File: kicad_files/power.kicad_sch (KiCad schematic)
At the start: 23 parts, among them J8 Conn_01x02_Socket, Q1 Q_PMOS_GSD, Q2 Q_PMOS_GSD, U11 LT1963AxST-3.3, U12 AP63205WU

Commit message: reset symbol annotations
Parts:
- renumbered C61 to C53, C62 to C54, C63 to C55, C64 to C56, C65 to C57, C66 to C58, C67 to C59, C68 to C60, C69 to C61, C70 to C62, C71 to C63, R25 to R22, R26 to R23, R27 to R24, R28 to R25
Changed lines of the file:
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@@
 		(dnp no)
 		(fields_autoplaced yes)
-		(property "Reference" "C70"
+		(property "Reference" "C62"
 			(at 161.29 127.0062 0)
 			(show_name no)
@@
 			(project "versorlite"
 				(path "/1a230af0-0a74-48f7-8607-b087121dda49/31c1824a-552d-4de4-ae9b-4526af07be04"
-					(reference "C70")
+					(reference "C62")
 					(unit 1)
 				)
@@
 		(dnp no)
 		(fields_autoplaced yes)
-		(property "Reference" "C62"
+		(property "Reference" "C54"
 			(at 46.9965 59.69 0)
 			(show_name no)
@@
 			(project "versorlite"
 				(path "/1a230af0-0a74-48f7-8607-b087121dda49/31c1824a-552d-4de4-ae9b-4526af07be04"
-					(reference "C62")
+					(reference "C54")
 					(unit 1)
 				)
@@
 		(dnp no)
 		(fields_autoplaced yes)
-		(property "Reference" "C68"
+		(property "Reference" "C60"
 			(at 107.95 134.6135 0)
 			(show_name no)
@@
 			(project "versorlite"
 				(path "/1a230af0-0a74-48f7-8607-b087121dda49/31c1824a-552d-4de4-ae9b-4526af07be04"
-					(reference "C68")
+					(reference "C60")
 					(unit 1)
 				)
@@
 		(dnp no)
 		(fields_autoplaced yes)
-		(property "Reference" "C67"
+		(property "Reference" "C59"
 			(at 107.95 124.4535 0)
 			(show_name no)
@@
 			(project "versorlite"
 				(path "/1a230af0-0a74-48f7-8607-b087121dda49/31c1824a-552d-4de4-ae9b-4526af07be04"
-					(reference "C67")
+					(reference "C59")
 					(unit 1)
 				)
@@
 		(dnp no)
 		(fields_autoplaced yes)
-		(property "Reference" "R25"
+		(property "Reference" "R22"
 			(at 54.61 154.9399 0)
 			(show_name no)
@@
 			(project "versorlite"
 				(path "/1a230af0-0a74-48f7-8607-b087121dda49/31c1824a-552d-4de4-ae9b-4526af07be04"
-					(reference "R25")
+					(reference "R22")
 					(unit 1)
 				)
@@
 		(dnp no)
 		(fields_autoplaced yes)
-		(property "Reference" "R28"
+		(property "Reference" "R25"
 			(at 180.34 143.5099 0)
 			(show_name no)
@@
 			(project "versorlite"
 				(path "/1a230af0-0a74-48f7-8607-b087121dda49/31c1824a-552d-4de4-ae9b-4526af07be04"
-					(reference "R28")
+					(reference "R25")
 					(unit 1)
 				)
@@
 		(dnp no)
 		(fields_autoplaced yes)
-		(property "Reference" "C61"
+		(property "Reference" "C53"
 			(at 46.9838 49.53 0)
 			(show_name no)
@@
 			(project "versorlite"
 				(path "/1a230af0-0a74-48f7-8607-b087121dda49/31c1824a-552d-4de4-ae9b-4526af07be04"
-					(reference "C61")
+					(reference "C53")
 					(unit 1)
 				)
@@
 		(dnp no)
 		(fields_autoplaced yes)
-		(property "Reference" "C69"
+		(property "Reference" "C61"
 			(at 151.13 126.9935 0)
 			(show_name no)
@@
 			(project "versorlite"
 				(path "/1a230af0-0a74-48f7-8607-b087121dda49/31c1824a-552d-4de4-ae9b-4526af07be04"
-					(reference "C69")
+					(reference "C61")
 					(unit 1)
 				)
@@
 		(dnp no)
 		(fields_autoplaced yes)
-		(property "Reference" "C66"
+		(property "Reference" "C58"
 			(at 97.79 124.4662 0)
 			(show_name no)
@@
 			(project "versorlite"
 				(path "/1a230af0-0a74-48f7-8607-b087121dda49/31c1824a-552d-4de4-ae9b-4526af07be04"
-					(reference "C66")
+					(reference "C58")
 					(unit 1)
 				)
@@
 		(dnp no)
 		(fields_autoplaced yes)
-		(property "Reference" "C63"
+		(property "Reference" "C55"
 			(at 45.7136 83.82 90)
 			(show_name no)
@@
 			(project "versorlite"
 				(path "/1a230af0-0a74-48f7-8607-b087121dda49/31c1824a-552d-4de4-ae9b-4526af07be04"
-					(reference "C63")
+					(reference "C55")
 					(unit 1)
 				)
@@
 		(in_pos_files yes)
 		(dnp no)
-		(property "Reference" "C71"
+		(property "Reference" "C63"
 			(at 163.83 138.938 0)
 			(show_name no)
@@
 			(project "versorlite"
 				(path "/1a230af0-0a74-48f7-8607-b087121dda49/31c1824a-552d-4de4-ae9b-4526af07be04"
-					(reference "C71")
+					(reference "C63")
 					(unit 1)
 				)
@@
 		(dnp no)
 		(fields_autoplaced yes)
-		(property "Reference" "C64"
+		(property "Reference" "C56"
 			(at 45.7263 93.98 90)
 			(show_name no)
@@
 			(project "versorlite"
 				(path "/1a230af0-0a74-48f7-8607-b087121dda49/31c1824a-552d-4de4-ae9b-4526af07be04"
-					(reference "C64")
+					(reference "C56")
 					(unit 1)
 				)
@@
 		(dnp no)
 		(fields_autoplaced yes)
-		(property "Reference" "R27"
+		(property "Reference" "R24"
 			(at 180.34 135.8899 0)
 			(show_name no)
@@
 			(project "versorlite"
 				(path "/1a230af0-0a74-48f7-8607-b087121dda49/31c1824a-552d-4de4-ae9b-4526af07be04"
-					(reference "R27")
+					(reference "R24")
 					(unit 1)
 				)
@@
 		(in_pos_files yes)
 		(dnp no)
-		(property "Reference" "R26"
+		(property "Reference" "R23"
 			(at 68.58 151.13 0)
 			(show_name no)
@@
 			(project "versorlite"
 				(path "/1a230af0-0a74-48f7-8607-b087121dda49/31c1824a-552d-4de4-ae9b-4526af07be04"
-					(reference "R26")
+					(reference "R23")
 					(unit 1)
 				)
@@
 		(dnp no)
 		(fields_autoplaced yes)
-		(property "Reference" "C65"
+		(property "Reference" "C57"
 			(at 80.01 124.4662 0)
 			(show_name no)
@@
 			(project "versorlite"
 				(path "/1a230af0-0a74-48f7-8607-b087121dda49/31c1824a-552d-4de4-ae9b-4526af07be04"
-					(reference "C65")
-					(unit 1)
-				)
+					(reference "C57")
+					(unit 1)
+				)

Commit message: make schematic changes
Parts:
- removed Q2: Q_PMOS_GSD, symbol Transistor_FET:Q_PMOS_GSD
- removed R23: 100Ω, symbol Device:R_Small_US
- added D8: D_Schottky_Small, symbol Device:D_Schottky_Small
- added SW3: SW_SPST, symbol Switch:SW_SPST
- Q1: value Q_PMOS_GSD -> JMTQ55P02A; footprint (none) -> Package_DFN_QFN:DFN-8-1EP_3x3mm_P0.65mm_EP1.6x2.56mm_ThermalVias
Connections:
- net +9V: now also SW3.2 (B); no longer F1.1
- net +VBUS: now also Q1.1 (G)
- net at C61.1, C62.2, C63.1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: now also D8.1 (K)
- net at F1.2: now also D8.2 (A)
- new net: F1.1, SW3.1 (A)
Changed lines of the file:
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@@
 	)
 	(junction
-		(at 193.04 142.24)
-		(diameter 0)
-		(color 0 0 0 0)
-	)
-	(junction
 		(at 182.88 134.62)
 		(diameter 0)
@@
 	(wire
 		(pts
+			(xy 63.5 147.32) (xy 63.5 152.4)
+		)
+		(stroke
+			(width 0)
+			(type default)
+		)
+	)
+	(wire
+		(pts
 			(xy 48.26 57.15) (xy 50.8 57.15)
 		)
@@
 	(wire
 		(pts
-			(xy 182.88 134.62) (xy 187.96 134.62)
+			(xy 182.88 134.62) (xy 190.5 134.62)
+		)
+		(stroke
+			(width 0)
+			(type default)
+		)
+	)
+	(wire
+		(pts
+			(xy 195.58 134.62) (xy 199.39 134.62)
 		)
 		(stroke
@@
 	(wire
 		(pts
-			(xy 198.12 134.62) (xy 199.39 134.62)
-		)
-		(stroke
-			(width 0)
-			(type default)
-		)
-	)
-	(wire
-		(pts
 			(xy 105.41 139.7) (xy 116.84 139.7)
 		)
@@
 	(symbol
 		(lib_id "power:+9V")
-		(at 210.82 134.62 270)
+		(at 220.98 134.62 270)
 		(unit 1)
 		(body_style 1)
@@
 		(fields_autoplaced yes)
 		(property "Reference" "#PWR091"
-			(at 207.01 134.62 0)
+			(at 217.17 134.62 0)
 			(hide yes)
 			(show_name no)
@@
 		)
 		(property "Value" "+9V"
-			(at 214.63 134.6199 90)
+			(at 224.79 134.6199 90)
 			(show_name no)
 			(do_not_autoplace no)
@@
 		)
 		(property "Footprint" ""
-			(at 210.82 134.62 0)
+			(at 220.98 134.62 0)
 			(hide yes)
 			(show_name no)
@@
 		)
 		(property "Datasheet" ""
-			(at 210.82 134.62 0)
+			(at 220.98 134.62 0)
 			(hide yes)
 			(show_name no)
@@
 		)
 		(property "Description" "Power symbol creates a global label with name \"+9V\""
-			(at 210.82 134.62 0)
+			(at 220.98 134.62 0)
 			(hide yes)
 			(show_name no)
@@
 	)
 	(symbol
+		(lib_id "Device:D_Schottky_Small")
+		(at 193.04 134.62 0)
+		(unit 1)
+		(body_style 1)
+		(exclude_from_sim no)
+		(in_bom yes)
+		(on_board yes)
+		(in_pos_files yes)
+		(dnp no)
+		(property "Reference" "D8"
+			(at 191.008 131.826 90)
+			(show_name no)
+			(do_not_autoplace no)
+			(effects
+				(font
+					(size 1.27 1.27)
+				)
+				(justify left)
+			)
+		)
+		(property "Value" "D_Schottky_Small"
+			(at 192.786 131.826 90)
+			(show_name no)
+			(do_not_autoplace no)
+			(effects
+				(font
+					(size 1.27 1.27)
+				)
+				(justify left)
+			)
+		)
+		(property "Footprint" ""
+			(at 193.04 134.62 90)
+			(hide yes)
+			(show_name no)
+			(do_not_autoplace no)
+			(effects
+				(font
+					(size 1.27 1.27)
+				)
+			)
+		)
+		(property "Datasheet" ""
+			(at 193.04 134.62 90)
+			(hide yes)
+			(show_name no)
+			(do_not_autoplace no)
+			(effects
+				(font
+					(size 1.27 1.27)
+				)
+			)
+		)
+		(property "Description" "Schottky diode, small symbol"
+			(at 193.04 134.62 0)
+			(hide yes)
+			(show_name no)
+			(do_not_autoplace no)
+			(effects
+				(font
+					(size 1.27 1.27)
+				)
+			)
+		)
+		(pin "1"
+		)
+		(pin "2"
+		)
+		(instances
+			(project "versorlite"
+				(path "/1a230af0-0a74-48f7-8607-b087121dda49/31c1824a-552d-4de4-ae9b-4526af07be04"
+					(reference "D8")
+					(unit 1)
+				)
+			)
+		)
+	)
+	(symbol
 		(lib_id "Device:C_Small")
 		(at 45.72 57.15 90)
@@
 			)
 		)
-		(property "Value" "Q_PMOS_GSD"
+		(property "Value" "JMTQ55P02A"
 			(at 63.5 135.89 90)
 			(show_name no)
@@
 			)
 		)
-		(property "Footprint" ""
+		(property "Footprint" "Package_DFN_QFN:DFN-8-1EP_3x3mm_P0.65mm_EP1.6x2.56mm_ThermalVias"
 			(at 60.96 137.16 0)
 			(hide yes)
@@
 	)
 	(symbol
-		(lib_id "Transistor_FET:Q_PMOS_GSD")
-		(at 193.04 137.16 90)
-		(unit 1)
-		(body_style 1)
-		(exclude_from_sim no)
-		(in_bom yes)
-		(on_board yes)
-		(in_pos_files yes)
-		(dnp no)
-		(fields_autoplaced yes)
-		(property "Reference" "Q2"
-			(at 193.04 128.27 90)
-			(show_name no)
-			(do_not_autoplace no)
-			(effects
-				(font
-					(size 1.27 1.27)
-				)
-			)
-		)
-		(property "Value" "Q_PMOS_GSD"
-			(at 193.04 130.81 90)
-			(show_name no)
-			(do_not_autoplace no)
-			(effects
-				(font
-					(size 1.27 1.27)
-				)
-			)
-		)
-		(property "Footprint" ""
-			(at 190.5 132.08 0)
-			(hide yes)
-			(show_name no)
-			(do_not_autoplace no)
-			(effects
-				(font
-					(size 1.27 1.27)
-				)
-			)
-		)
-		(property "Datasheet" ""
-			(at 193.04 137.16 0)
-			(hide yes)
-			(show_name no)
-			(do_not_autoplace no)
-			(effects
-				(font
-					(size 1.27 1.27)
-				)
-			)
-		)
-		(property "Description" "P-MOSFET transistor, gate/source/drain"
-			(at 193.04 137.16 0)
-			(hide yes)
-			(show_name no)
-			(do_not_autoplace no)
-			(effects
-				(font
-					(size 1.27 1.27)
-				)
-			)
-		)
-		(pin "3"
-		)
-		(pin "1"
-		)
-		(pin "2"
-		)
-		(instances
-			(project "versorlite"
-				(path "/1a230af0-0a74-48f7-8607-b087121dda49/31c1824a-552d-4de4-ae9b-4526af07be04"
-					(reference "Q2")
-					(unit 1)
-				)
-			)
-		)
-	)
-	(symbol
 		(lib_id "power:GND")
 		(at 196.85 142.24 90)
@@
 	)
 	(symbol
-		(lib_id "Device:R_Small_US")
-		(at 63.5 149.86 0)
+		(lib_id "power:+3.3V")
+		(at 40.64 38.1 0)
 		(unit 1)
 		(body_style 1)
@@
 		(in_pos_files yes)
 		(dnp no)
-		(property "Reference" "R23"
-			(at 68.58 151.13 0)
+		(property "Reference" "#PWR085"
+			(at 40.64 41.91 0)
+			(hide yes)
 			(show_name no)
 			(do_not_autoplace no)
@@
 			)
 		)
-		(property "Value" "100Ω"
-			(at 68.58 148.59 0)
+		(property "Value" "+3.3V_MAIN"
+			(at 40.386 33.782 0)
 			(show_name no)
 			(do_not_autoplace no)
@@
 		)
 		(property "Footprint" ""
-			(at 63.5 149.86 0)
+			(at 40.64 38.1 0)
 			(hide yes)
 			(show_name no)
@@
 		)
 		(property "Datasheet" ""
-			(at 63.5 149.86 0)
+			(at 40.64 38.1 0)
 			(hide yes)
 			(show_name no)
@@
 			)
 		)
-		(property "Description" "Resistor, small US symbol"
-			(at 63.5 149.86 0)
+		(property "Description" "Power symbol creates a global label with name \"+3.3V\""
+			(at 40.64 38.1 0)
 			(hide yes)
 			(show_name no)
@@
 			)
 		)
-		(pin "2"
-		)
 		(pin "1"
 		)
@@
 			(project "versorlite"
 				(path "/1a230af0-0a74-48f7-8607-b087121dda49/31c1824a-552d-4de4-ae9b-4526af07be04"
-					(reference "R23")
+					(reference "#PWR085")
 					(unit 1)
 				)
@@
 	)
 	(symbol
-		(lib_id "power:+3.3V")
-		(at 40.64 38.1 0)
+		(lib_id "Device:C_Small")
+		(at 77.47 125.73 0)
 		(unit 1)
 		(body_style 1)
@@
 		(in_pos_files yes)
 		(dnp no)
-		(property "Reference" "#PWR085"
-			(at 40.64 41.91 0)
-			(hide yes)
+		(fields_autoplaced yes)
+		(property "Reference" "C57"
+			(at 80.01 124.4662 0)
 			(show_name no)
 			(do_not_autoplace no)
@@
 					(size 1.27 1.27)
 				)
+				(justify left)
 			)
 		)
-		(property "Value" "+3.3V_MAIN"
-			(at 40.386 33.782 0)
+		(property "Value" "100μf"
+			(at 80.01 127.0062 0)
 			(show_name no)
 			(do_not_autoplace no)
@@
 					(size 1.27 1.27)
 				)
+				(justify left)
 			)
 		)
-		(property "Footprint" ""
-			(at 40.64 38.1 0)
+		(property "Footprint" "Capacitor_Tantalum_SMD:CP_EIA-3528-21_Kemet-B"
+			(at 77.47 125.73 0)
 			(hide yes)
 			(show_name no)
@@
 		)
 		(property "Datasheet" ""
-			(at 40.64 38.1 0)
+			(at 77.47 125.73 0)
 			(hide yes)
 			(show_name no)
@@
 			)
 		)
-		(property "Description" "Power symbol creates a global label with name \"+3.3V\""
-			(at 40.64 38.1 0)
+		(property "Description" "Unpolarized capacitor, small symbol"
+			(at 77.47 125.73 0)
 			(hide yes)
 			(show_name no)
@@
 		(pin "1"
 		)
+		(pin "2"
+		)
 		(instances
 			(project "versorlite"
 				(path "/1a230af0-0a74-48f7-8607-b087121dda49/31c1824a-552d-4de4-ae9b-4526af07be04"
-					(reference "#PWR085")
+					(reference "C57")
 					(unit 1)
 				)
@@
 	)
 	(symbol
-		(lib_id "Device:C_Small")
-		(at 77.47 125.73 0)
+		(lib_id "Switch:SW_SPST")
+		(at 215.9 134.62 0)
 		(unit 1)
 		(body_style 1)
@@
 		(dnp no)
 		(fields_autoplaced yes)
-		(property "Reference" "C57"
-			(at 80.01 124.4662 0)
+		(property "Reference" "SW3"
+			(at 215.9 128.27 0)
 			(show_name no)
 			(do_not_autoplace no)
@@
 					(size 1.27 1.27)
 				)
-				(justify left)
 			)
 		)
-		(property "Value" "100μf"
-			(at 80.01 127.0062 0)
+		(property "Value" "SW_SPST"
+			(at 215.9 130.81 0)
 			(show_name no)
 			(do_not_autoplace no)
@@
 					(size 1.27 1.27)
 				)
-				(justify left)
 			)
 		)
-		(property "Footprint" "Capacitor_Tantalum_SMD:CP_EIA-3528-21_Kemet-B"
-			(at 77.47 125.73 0)
+		(property "Footprint" ""
+			(at 215.9 134.62 0)
 			(hide yes)
 			(show_name no)
@@
 		)
 		(property "Datasheet" ""
-			(at 77.47 125.73 0)
+			(at 215.9 134.62 0)
 			(hide yes)
 			(show_name no)
@@
 			)
 		)
-		(property "Description" "Unpolarized capacitor, small symbol"
-			(at 77.47 125.73 0)
+		(property "Description" "Single Pole Single Throw (SPST) switch"
+			(at 215.9 134.62 0)
 			(hide yes)
 			(show_name no)
@@
 			(project "versorlite"
 				(path "/1a230af0-0a74-48f7-8607-b087121dda49/31c1824a-552d-4de4-ae9b-4526af07be04"
-					(reference "C57")
+					(reference "SW3")
 					(unit 1)
 				)

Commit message: add footprint
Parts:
- Q1: value JMTQ55P02A -> FDMC510P-MS
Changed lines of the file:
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@@
 			)
 		)
-		(property "Value" "JMTQ55P02A"
+		(property "Value" "FDMC510P-MS"
 			(at 63.5 135.89 90)
 			(show_name no)
@@
 			)
 		)
+		(pin "1"
+		)
 		(pin "3"
 		)
-		(pin "1"
-		)
 		(pin "2"

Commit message: Rearrange PCB
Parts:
- J8: footprint (none) -> Connector_AMASS:AMASS_XT30U-F_1x02_P5.0mm_Vertical
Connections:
- net +9V: now also J8.2 (Pin_2); no longer J8.1 (Pin_1)
- net GND: now also J8.1 (Pin_1); no longer J8.2 (Pin_2)
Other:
- moved on the sheet: J8

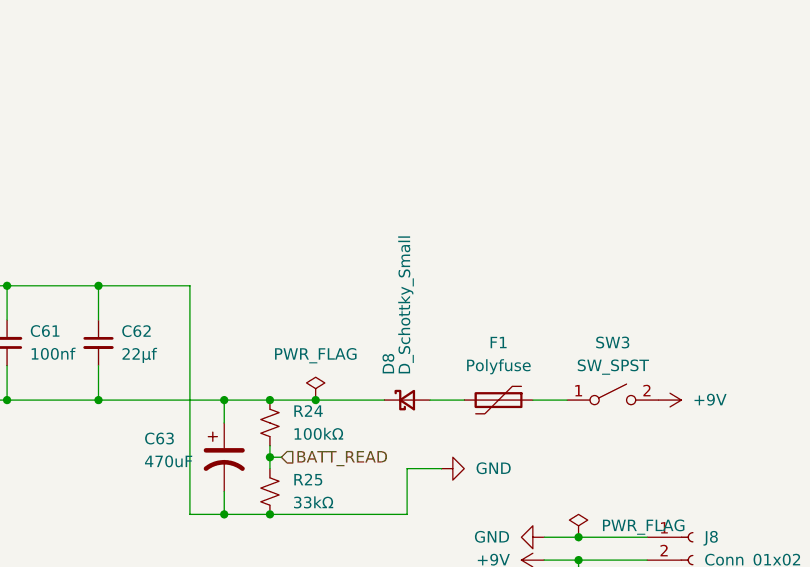
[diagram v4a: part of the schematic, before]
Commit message: VBUS, BMS diodes and fuses
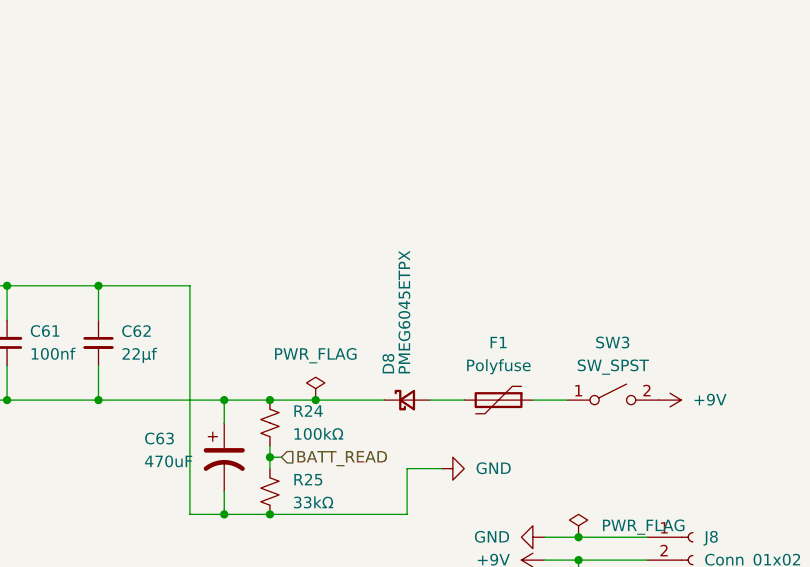
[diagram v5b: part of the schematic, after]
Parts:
- D8: value D_Schottky_Small -> PMEG6045ETPX; footprint (none) -> Diode_SMD:D_SOD-128
- F1: footprint (none) -> Fuse:Fuse_1812_4532Metric
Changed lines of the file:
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@@
 			)
 		)
-		(property "Value" "D_Schottky_Small"
+		(property "Value" "PMEG6045ETPX"
 			(at 192.786 131.826 90)
 			(show_name no)
@@
 			)
 		)
-		(property "Footprint" ""
+		(property "Footprint" "Diode_SMD:D_SOD-128"
 			(at 193.04 134.62 90)
 			(hide yes)
@@
 			)
 		)
-		(property "Footprint" ""
+		(property "Footprint" "Fuse:Fuse_1812_4532Metric"
 			(at 198.12 135.89 0)
 			(hide yes)

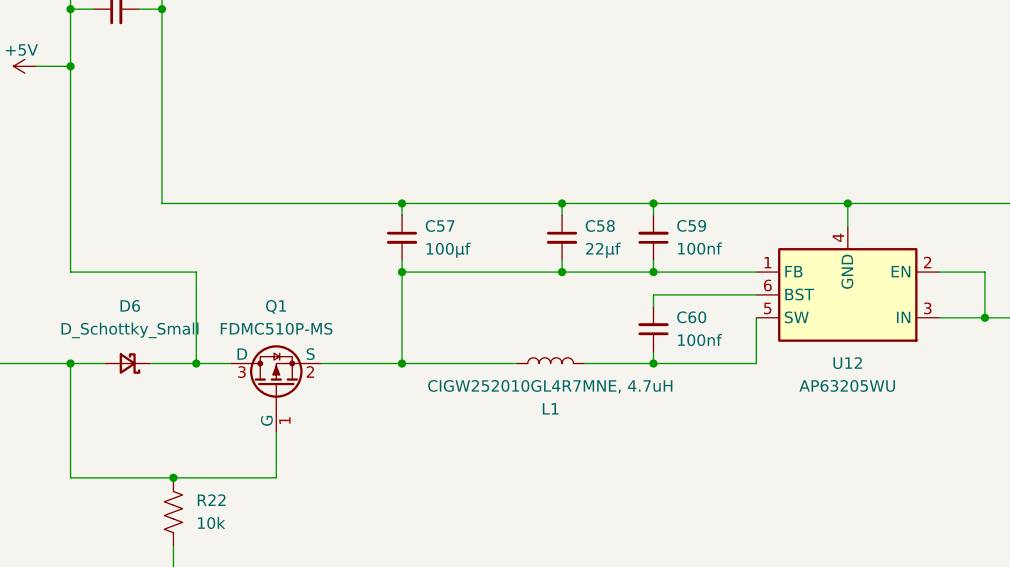
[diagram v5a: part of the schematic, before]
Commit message: fix mcu decaps
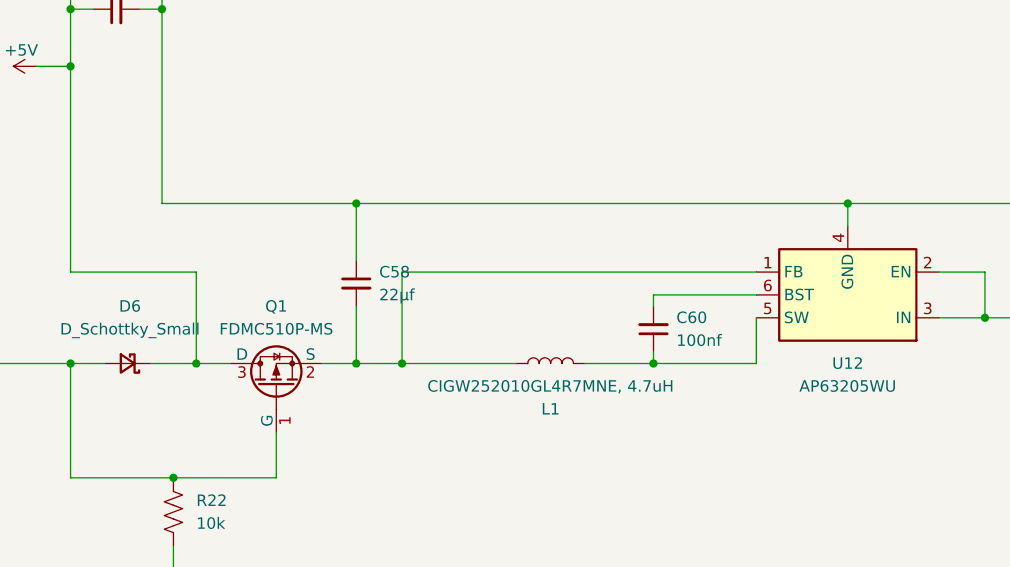
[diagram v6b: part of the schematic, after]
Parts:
- removed C57: 100μf, Capacitor_Tantalum_SMD:CP_EIA-3528-21_Kemet-B, symbol Device:C_Small
- removed C59: 100nf, Capacitor_SMD:C_0402_1005Metric, symbol Device:C_Small
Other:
- moved on the sheet: C58
